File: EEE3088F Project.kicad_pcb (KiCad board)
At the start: 2 copper layers, 60 x 82 mm, 84 parts, among them J1 Conn_02x16_Odd_Even, J2 Battery IN JST, M1BulkC1 10uF, M1Control1 DRV8837, M2BulkC1 10uF, M2Control1 DRV8837, M3BulkC1 10uF, M3Control1 DRV8837, M4BulkC1 10uF, M4Control1 DRV8837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

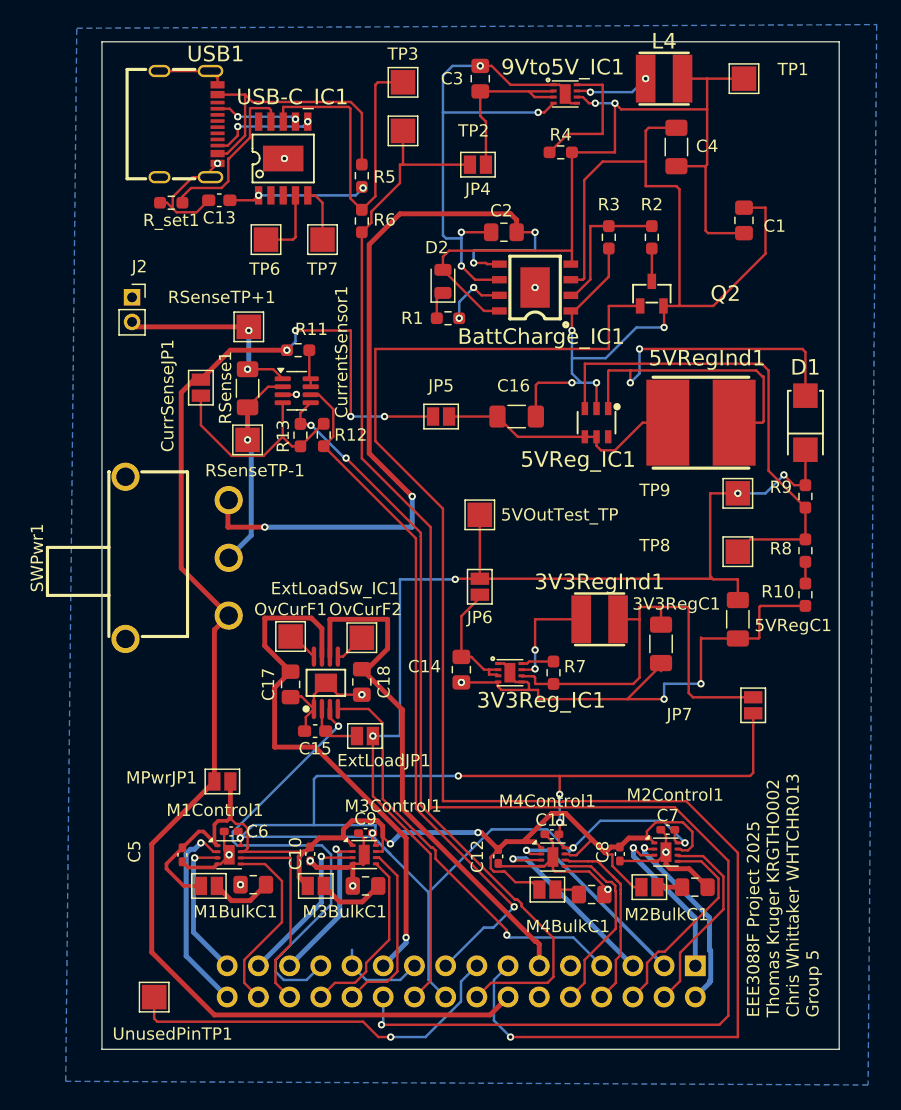
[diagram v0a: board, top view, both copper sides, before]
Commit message: added thicker lines for 9V, 5V, VBatt and 3V3
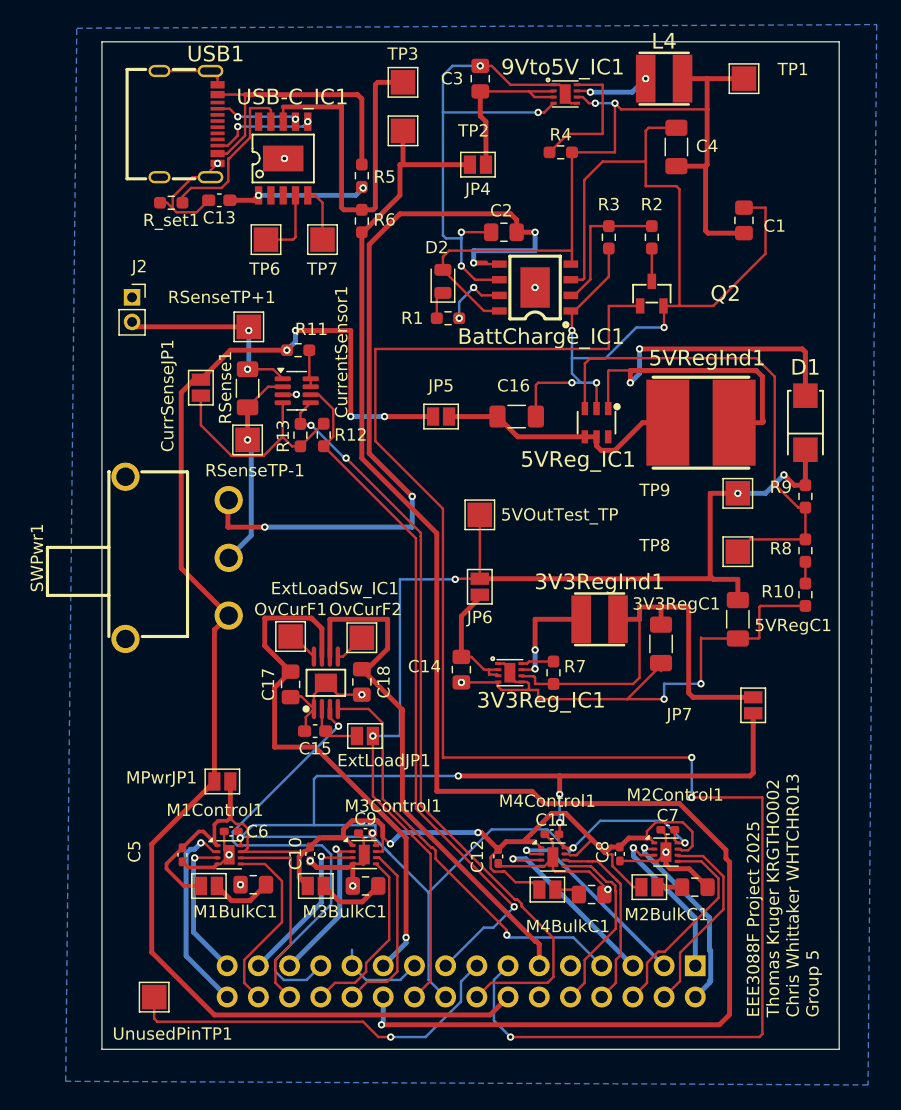
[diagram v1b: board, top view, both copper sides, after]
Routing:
- net /FAST_CHRG_CNTRL: track 130.2 -> 136.7 mm, vias 1 -> 3
- net Net-(USB-C_IC1-VBUS): track 28.3 -> 29.4 mm
- net Net-(5VReg_IC1-FB): track 39.7 -> 40.5 mm
- net /VBUS_USBC: track 22.9 -> 23.6 mm
- net 9V USB-C: track 134.0 -> 133.3 mm

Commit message: Finishing touches + mounting hole
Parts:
- added REF**: MountingHole_2.1mm, MountingHole:MountingHole_2.1mm, F.Cu at (178.8, 84.3)
- moved 5VOutTest_TP 8.32 mm to (187.3, 85.4)
- moved JP6 1.44 mm to (180.9, 88.7)
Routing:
- net /FAST_CHRG_CNTRL: track 136.7 -> 131.7 mm
- net /5V Regulated: track 91.7 -> 95.3 mm
- net Net-(3V3Reg_IC1-EN): track 10.3 -> 11.5 mm
